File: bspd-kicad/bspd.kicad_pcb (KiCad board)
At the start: 2 copper layers, 6 parts

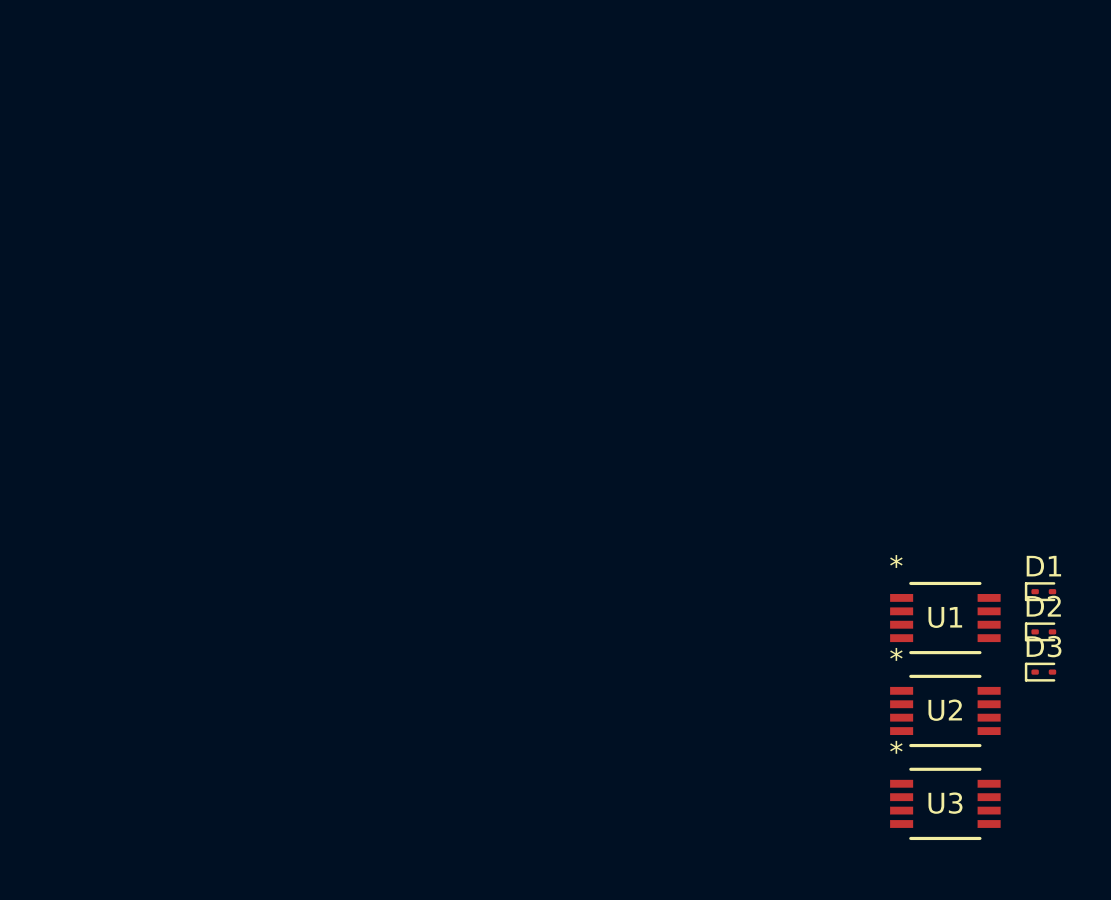
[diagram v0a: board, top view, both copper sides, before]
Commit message: fixed foot print, added power and connector
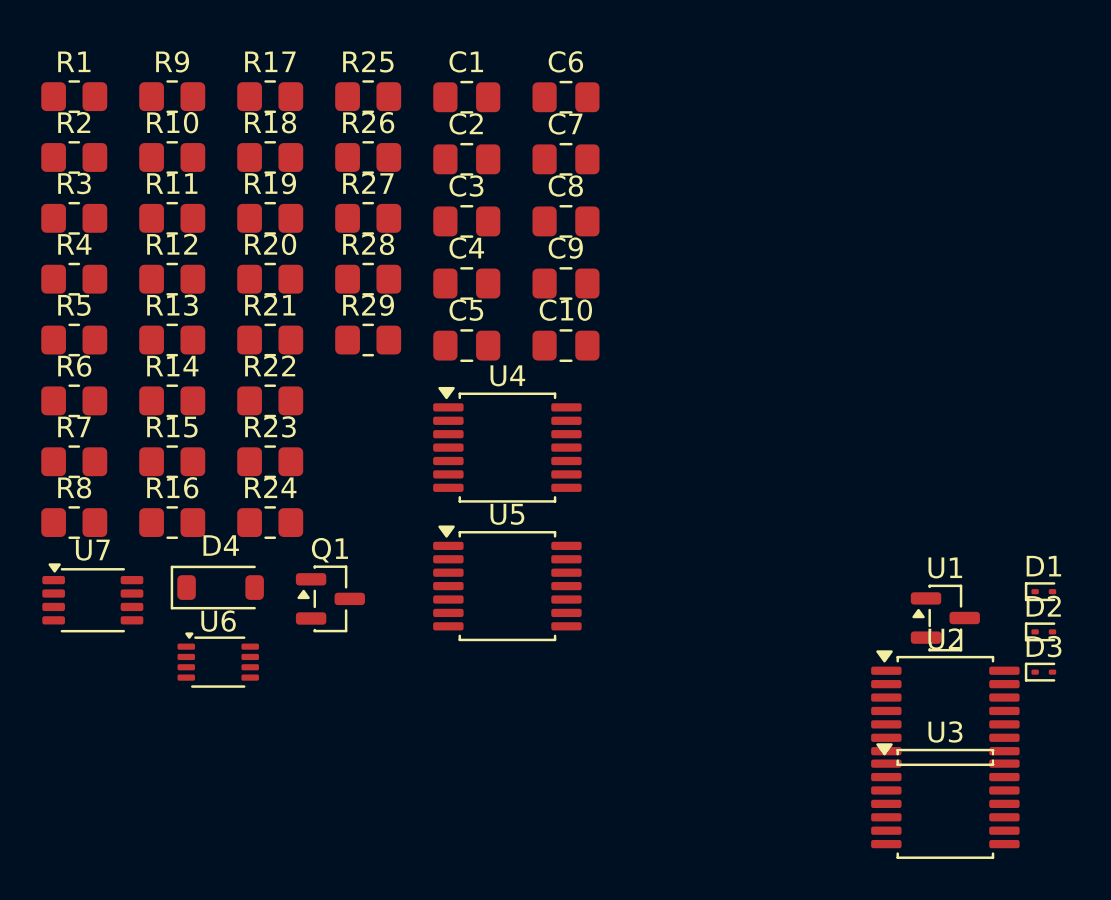
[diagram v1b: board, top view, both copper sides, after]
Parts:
- added C1: 1uF, Capacitor_SMD:C_0805_2012Metric_Pad1.18x1.45mm_HandSolder, F.Cu at (47.2, 34.5)
- added C10: xuF, Capacitor_SMD:C_0805_2012Metric_Pad1.18x1.45mm_HandSolder, F.Cu at (52.0, 46.5)
- added C2: 1uF, Capacitor_SMD:C_0805_2012Metric_Pad1.18x1.45mm_HandSolder, F.Cu at (47.2, 37.5)
- added C3: 5uF, Capacitor_SMD:C_0805_2012Metric_Pad1.18x1.45mm_HandSolder, F.Cu at (47.2, 40.5)
- added C4: 1uF, Capacitor_SMD:C_0805_2012Metric_Pad1.18x1.45mm_HandSolder, F.Cu at (47.2, 43.5)
- added C5: 1uF, Capacitor_SMD:C_0805_2012Metric_Pad1.18x1.45mm_HandSolder, F.Cu at (47.2, 46.5)
- added C6: 1uF, Capacitor_SMD:C_0805_2012Metric_Pad1.18x1.45mm_HandSolder, F.Cu at (52.0, 34.5)
- added C7: 1uF, Capacitor_SMD:C_0805_2012Metric_Pad1.18x1.45mm_HandSolder, F.Cu at (52.0, 37.5)
- added C8: 1uF, Capacitor_SMD:C_0805_2012Metric_Pad1.18x1.45mm_HandSolder, F.Cu at (52.0, 40.5)
- added C9: 1uF, Capacitor_SMD:C_0805_2012Metric_Pad1.18x1.45mm_HandSolder, F.Cu at (52.0, 43.5)
- added D4: 1N4148W, Diode_SMD:D_SOD-123, F.Cu at (35.2, 58.3)
- added Q1: AO3400A, Package_TO_SOT_SMD:SOT-23, F.Cu at (40.5, 58.8)
- added R1: 10k, Resistor_SMD:R_0805_2012Metric_Pad1.20x1.40mm_HandSolder, F.Cu at (28.1, 34.5)
- added R10: 10k, Resistor_SMD:R_0805_2012Metric_Pad1.20x1.40mm_HandSolder, F.Cu at (32.9, 37.4)
- added R11: 150k, Resistor_SMD:R_0805_2012Metric_Pad1.20x1.40mm_HandSolder, F.Cu at (32.9, 40.4)
- added R12: 150k, Resistor_SMD:R_0805_2012Metric_Pad1.20x1.40mm_HandSolder, F.Cu at (32.9, 43.3)
- added R13: 5.1k, Resistor_SMD:R_0805_2012Metric_Pad1.20x1.40mm_HandSolder, F.Cu at (32.9, 46.3)
- added R14: 150k, Resistor_SMD:R_0805_2012Metric_Pad1.20x1.40mm_HandSolder, F.Cu at (32.9, 49.2)
- added R15: 10k, Resistor_SMD:R_0805_2012Metric_Pad1.20x1.40mm_HandSolder, F.Cu at (32.9, 52.2)
- added R16: 150k, Resistor_SMD:R_0805_2012Metric_Pad1.20x1.40mm_HandSolder, F.Cu at (32.9, 55.1)
- added R17: 5.1k, Resistor_SMD:R_0805_2012Metric_Pad1.20x1.40mm_HandSolder, F.Cu at (37.6, 34.5)
- added R18: 150k, Resistor_SMD:R_0805_2012Metric_Pad1.20x1.40mm_HandSolder, F.Cu at (37.6, 37.4)
- added R19: 150k, Resistor_SMD:R_0805_2012Metric_Pad1.20x1.40mm_HandSolder, F.Cu at (37.6, 40.4)
- added R2: 5.1k, Resistor_SMD:R_0805_2012Metric_Pad1.20x1.40mm_HandSolder, F.Cu at (28.1, 37.4)
- added R20: 5.1k, Resistor_SMD:R_0805_2012Metric_Pad1.20x1.40mm_HandSolder, F.Cu at (37.6, 43.3)
- added R21: 54.9k, Resistor_SMD:R_0805_2012Metric_Pad1.20x1.40mm_HandSolder, F.Cu at (37.6, 46.3)
- added R22: 21.5k, Resistor_SMD:R_0805_2012Metric_Pad1.20x1.40mm_HandSolder, F.Cu at (37.6, 49.2)
- added R23: 100k, Resistor_SMD:R_0805_2012Metric_Pad1.20x1.40mm_HandSolder, F.Cu at (37.6, 52.2)
- added R24: 4.99k, Resistor_SMD:R_0805_2012Metric_Pad1.20x1.40mm_HandSolder, F.Cu at (37.6, 55.1)
- added R25: 5.49k, Resistor_SMD:R_0805_2012Metric_Pad1.20x1.40mm_HandSolder, F.Cu at (42.4, 34.5)
- added R26: 7.15k, Resistor_SMD:R_0805_2012Metric_Pad1.20x1.40mm_HandSolder, F.Cu at (42.4, 37.4)
- added R27: 100k, Resistor_SMD:R_0805_2012Metric_Pad1.20x1.40mm_HandSolder, F.Cu at (42.4, 40.4)
- added R28: 45.3k, Resistor_SMD:R_0805_2012Metric_Pad1.20x1.40mm_HandSolder, F.Cu at (42.4, 43.3)
- added R29: x, Resistor_SMD:R_0805_2012Metric_Pad1.20x1.40mm_HandSolder, F.Cu at (42.4, 46.3)
- added R3: 5.1k, Resistor_SMD:R_0805_2012Metric_Pad1.20x1.40mm_HandSolder, F.Cu at (28.1, 40.4)
- added R4: 150k, Resistor_SMD:R_0805_2012Metric_Pad1.20x1.40mm_HandSolder, F.Cu at (28.1, 43.3)
- added R5: 5.1k, Resistor_SMD:R_0805_2012Metric_Pad1.20x1.40mm_HandSolder, F.Cu at (28.1, 46.3)
- added R6: 150k, Resistor_SMD:R_0805_2012Metric_Pad1.20x1.40mm_HandSolder, F.Cu at (28.1, 49.2)
- added R7: 150k, Resistor_SMD:R_0805_2012Metric_Pad1.20x1.40mm_HandSolder, F.Cu at (28.1, 52.2)
- added R8: 150k, Resistor_SMD:R_0805_2012Metric_Pad1.20x1.40mm_HandSolder, F.Cu at (28.1, 55.1)
- added R9: 5.1k, Resistor_SMD:R_0805_2012Metric_Pad1.20x1.40mm_HandSolder, F.Cu at (32.9, 34.5)
- added U4: ~, bspd:TLV1704, F.Cu at (49.1, 51.5)
- added U5: ~, bspd:TLV1704, F.Cu at (49.1, 58.2)
- added U6: SN74LVC3G14DCUR, bspd:SN74LVC3G14DCUR, F.Cu at (35.1, 61.9)
- added U7: SN74LVC2G00DCTR, bspd:SN74LVC2G00DCTR, F.Cu at (29.0, 58.9)
- U1: value ~ -> MCP1703T-5002E/CB; footprint bspd:TLV3202AQDGKRQ1 -> bspd:MCP1703T-5002E-CB
- U2, U3: footprint bspd:TLV3202AQDGKRQ1 -> bspd:TLV1704
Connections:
- U1 pad 1: Net-(D4-A) -> Earth
- U1 pad 2: TPS1 -> +5V
- U1 pad 3: +4.5V -> +12V
- U2 pad 1: Net-(D6-A) -> TPS1_FAULT
- U2 pad 2: TPS2 -> TPS1_FAULT
- U2 pad 3: +4.5V -> +5V
- U2 pad 4: Earth -> TPS1
- U2 pad 5: TPS2 -> +4V5
- U2 pad 6: +0.5V -> +0V45
- U2 pad 7: Net-(D7-A) -> TPS1
- U2 pad 8: +5V -> TPS2
- U3 pad 1: Net-(D8-A) -> BPS_FAULT
- U3 pad 2: BPS -> BPS_FAULT
- U3 pad 3: +4.5V -> +5V
- U3 pad 4: Earth -> BPS
- U3 pad 5: BPS -> +4V5
- U3 pad 6: +0.5V -> +0V45
- U3 pad 7: Net-(D9-A) -> BPS
- U3 pad 8: +5V -> BPS

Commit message: Begun layout
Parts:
- moved U1 66.5 mm to (19.7, 16.7)
- moved R9 65.5 mm to (63.2, 92.5), turned to -90 degrees
- moved R19 64.6 mm to (78.0, 90.8), turned to 90 degrees
- moved R5 64.2 mm to (81.5, 82.0), turned to 90 degrees
- moved R3 57.6 mm to (53.2, 92.2), turned to -90 degrees
- moved C6 57.1 mm to (73.2, 87.5)
- moved R14 57.0 mm to (72.2, 90.5), turned to 90 degrees
- moved C7 56.5 mm to (37.0, 92.0), turned to -90 degrees
- moved R11 55.9 mm to (56.5, 91.0), turned to 180 degrees
- moved R13 54.8 mm to (56.5, 95.8), turned to 180 degrees
- moved R18 54.6 mm to (78.0, 74.2), turned to -90 degrees
- moved D3 53.4 mm to (31.5, 93.2), turned to 90 degrees
- moved R6 52.4 mm to (56.5, 93.2), turned to 180 degrees
- moved C9 51.6 mm to (79.0, 87.5)
- moved D2 50.2 mm to (31.5, 85.2), turned to 90 degrees
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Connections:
- C3 pad 1: Net-(U4C-+) -> Net-(U5A-+)
- C6 pad 1: Net-(U4D-+) -> Net-(U5B-+)
- C8 pad 1: Net-(U5A-+) -> Net-(U5C-+)
- C9 pad 1: Net-(U5B-+) -> Net-(U5D-+)
- R14 pad 2: Net-(U4D-+) -> Net-(U5B-+)
- R18 pad 2: Net-(U5A-+) -> Net-(U5C-+)
- R19 pad 2: Net-(U5B-+) -> Net-(U5D-+)
- R8 pad 2: Net-(U4C-+) -> Net-(U5A-+)
- U4 pad 10: +2V5 -> Earth
- U4 pad 11: Net-(U4D-+) -> +5V
- U4 pad 13: FAULT -> unconnected-(U4-Pad13)
- U4 pad 14: FAULT -> unconnected-(U4-Pad14)
- U4 pad 8: +2V5 -> Earth
- U4 pad 9: Net-(U4C-+) -> +5V
- U5 pad 10: Earth -> +2V5
- U5 pad 11: +5V -> Net-(U5D-+)
- U5 pad 13: unconnected-(U5-Pad13) -> FAULT
- U5 pad 14: unconnected-(U5-Pad14) -> FAULT
- U5 pad 8: Earth -> +2V5
- U5 pad 9: +5V -> Net-(U5C-+)

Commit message: Switched to D latch chip
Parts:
- removed U6: SN74LVC3G14DCUR, bspd:SN74LVC3G14DCUR
- C10: value xuF -> 2.2uF
- R29: value x -> 330k
- U7: value SN74LVC2G00DCTR -> SN74LVC2G14DBVR; footprint bspd:SN74LVC2G00DCTR -> bspd:SN74LVC2G14DBVR
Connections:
- U7 pad 1: Net-(U7A-A) -> Net-(D4-A)
- U7 pad 2: Net-(U7A-B) -> Earth
- U7 pad 3: Net-(U7A-B) -> Net-(U7-Pad3)
- U7 pad 4: Earth -> Net-(U8A-~{R})
- U7 pad 5: Net-(Q1-G) -> +5V
- U7 pad 6: Net-(U7B-B) -> Net-(U7-Pad3)

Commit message: Fixed latch and added indicator LEDs
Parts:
- removed C10: 2.2uF, Capacitor_SMD:C_0805_2012Metric_Pad1.18x1.45mm_HandSolder
- removed Q1: AO3400A, Package_TO_SOT_SMD:SOT-23
- added C11: 5uF, Capacitor_SMD:C_0805_2012Metric_Pad1.18x1.45mm_HandSolder, F.Cu at (24.9, 54.5)
- added D10: AP2012EC, bspd:AP2012EC, F.Cu at (76.4, 48.2)
- added D11: AP2012EC, bspd:AP2012EC, F.Cu at (76.4, 51.8)
- added D5: AP2012EC, bspd:AP2012EC, F.Cu at (76.4, 30.8)
- added D6: AP2012EC, bspd:AP2012EC, F.Cu at (76.4, 34.2)
- added D7: AP2012EC, bspd:AP2012EC, F.Cu at (76.4, 37.8)
- added D8: AP2012EC, bspd:AP2012EC, F.Cu at (76.4, 41.2)
- added D9: AP2012EC, bspd:AP2012EC, F.Cu at (76.4, 44.8)
- added Q2: AO3401A, Package_TO_SOT_SMD:SOT-23, F.Cu at (5.31, 59.2)
- added R30: 150k, Resistor_SMD:R_0805_2012Metric_Pad1.20x1.40mm_HandSolder, F.Cu at (24.9, 57.5)
- added R31: 300, Resistor_SMD:R_0805_2012Metric_Pad1.20x1.40mm_HandSolder, F.Cu at (71.8, 30.8)
- added R32: 300, Resistor_SMD:R_0805_2012Metric_Pad1.20x1.40mm_HandSolder, F.Cu at (71.8, 34.2)
- added R33: 300, Resistor_SMD:R_0805_2012Metric_Pad1.20x1.40mm_HandSolder, F.Cu at (71.8, 37.8)
- added R34: 300, Resistor_SMD:R_0805_2012Metric_Pad1.20x1.40mm_HandSolder, F.Cu at (71.8, 41.2)
- added R35: 300, Resistor_SMD:R_0805_2012Metric_Pad1.20x1.40mm_HandSolder, F.Cu at (71.8, 44.8)
- added R36: 300, Resistor_SMD:R_0805_2012Metric_Pad1.20x1.40mm_HandSolder, F.Cu at (71.8, 48.2)
- added R37: 300, Resistor_SMD:R_0805_2012Metric_Pad1.20x1.40mm_HandSolder, F.Cu at (71.8, 51.8)
- added R38: 300, Resistor_SMD:R_0805_2012Metric_Pad1.20x1.40mm_HandSolder, F.Cu at (-0.25, 58.2)
- added RV4: 3313J-1-103E, bspd:3313J-1-103E, F.Cu at (16.5, 49.6)
- added RV5: 3313J-1-103E, bspd:3313J-1-103E, F.Cu at (21.4, 49.6)
- added RV6: 3313J-1-103E, bspd:3313J-1-103E, F.Cu at (26.4, 49.6)
- added U6: SN74HC74DR, bspd:SN74HC74DR, F.Cu at (18.2, 58.3)
- added U8: SN74LVC3G14DCUR, bspd:SN74LVC3G14DCUR, F.Cu at (84.5, 33.5)
- added U9: SN74LVC3G14DCUR, bspd:SN74LVC3G14DCUR, F.Cu at (84.5, 44.0)
- R29: value 330k -> 150k
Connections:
- net Net-(R11-Pad2) renamed TPSx10%
- net Net-(U4B-+) renamed HB
- R29 pad 1: Net-(D4-A) -> Net-(R29-Pad1)
- R29 pad 2: +5V -> Net-(D4-A)

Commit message: Started layout, emphasis on looking good
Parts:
- removed RV6: 3313J-1-103E, bspd:3313J-1-103E
- removed U6: SN74HC74DR, bspd:SN74HC74DR
- added C10: 4.7uF, Capacitor_SMD:C_0805_2012Metric_Pad1.18x1.45mm_HandSolder, F.Cu at (102.9, 49.7)
- added C12: 100nF, Capacitor_SMD:C_0805_2012Metric_Pad1.18x1.45mm_HandSolder, F.Cu at (13.5, 16.0)
- added C13: 100nF, Capacitor_SMD:C_0805_2012Metric_Pad1.18x1.45mm_HandSolder, F.Cu at (101.2, 60.5)
- added C14: 100nF, Capacitor_SMD:C_0805_2012Metric_Pad1.18x1.45mm_HandSolder, F.Cu at (101.2, 63.5)
- added C15: 100nF, Capacitor_SMD:C_0805_2012Metric_Pad1.18x1.45mm_HandSolder, F.Cu at (101.2, 66.5)
- added C16: 100nF, Capacitor_SMD:C_0805_2012Metric_Pad1.18x1.45mm_HandSolder, F.Cu at (101.2, 69.5)
- added C17: 100nF, Capacitor_SMD:C_0805_2012Metric_Pad1.18x1.45mm_HandSolder, F.Cu at (101.2, 72.6)
- added C18: 100nF, Capacitor_SMD:C_0805_2012Metric_Pad1.18x1.45mm_HandSolder, F.Cu at (101.2, 75.6)
- added C19: 4.7uF, Capacitor_SMD:C_0805_2012Metric_Pad1.18x1.45mm_HandSolder, F.Cu at (98.9, 91.0)
- added C20: 100nF, Capacitor_SMD:C_0805_2012Metric_Pad1.18x1.45mm_HandSolder, F.Cu at (98.9, 94.0)
- added C21: 100nF, Capacitor_SMD:C_0805_2012Metric_Pad1.18x1.45mm_HandSolder, F.Cu at (98.9, 97.0)
- added C22: 100nF, Capacitor_SMD:C_0805_2012Metric_Pad1.18x1.45mm_HandSolder, F.Cu at (98.9, 100.0)
- added C23: 100nF, Capacitor_SMD:C_0805_2012Metric_Pad1.18x1.45mm_HandSolder, F.Cu at (98.9, 103.0)
- added C24: 100nF, Capacitor_SMD:C_0805_2012Metric_Pad1.18x1.45mm_HandSolder, F.Cu at (103.7, 91.0)
- added C25: 100nF, Capacitor_SMD:C_0805_2012Metric_Pad1.18x1.45mm_HandSolder, F.Cu at (103.7, 94.0)
- added C26: 100nF, Capacitor_SMD:C_0805_2012Metric_Pad1.18x1.45mm_HandSolder, F.Cu at (103.7, 97.0)
- added C27: 100nF, Capacitor_SMD:C_0805_2012Metric_Pad1.18x1.45mm_HandSolder, F.Cu at (103.7, 100.0)
- added C28: 100nF, Capacitor_SMD:C_0805_2012Metric_Pad1.18x1.45mm_HandSolder, F.Cu at (103.7, 103.0)
- added D12: AP2012EC, bspd:AP2012EC, F.Cu at (103.0, 39.4)
- added D13: AP2012EC, bspd:AP2012EC, F.Cu at (103.0, 42.3)
- added D14: 1N4148W, Diode_SMD:D_SOD-123, F.Cu at (109.0, 99.5)
- added Q1: AO3401A, Package_TO_SOT_SMD:SOT-23, F.Cu at (102.9, 45.9)
- added R39: 47k, Resistor_SMD:R_0805_2012Metric_Pad1.20x1.40mm_HandSolder, F.Cu at (107.7, 45.2)
- added R40: 56k, Resistor_SMD:R_0805_2012Metric_Pad1.20x1.40mm_HandSolder, F.Cu at (107.7, 48.1)
- added RV1: 3313J-1-203E, bspd:3313J-1-103E, F.Cu at (96.0, 34.6)
- added RV2: 3313J-1-203E, bspd:3313J-1-103E, F.Cu at (100.9, 34.6)
- added RV3: 3313J-1-203E, bspd:3313J-1-103E, F.Cu at (105.9, 34.6)
- added SW1: CJS-1200TB1, bspd:CJS-1200TB1, F.Cu at (97.0, 41.4)
- added SW2: CJS-1200TB1, bspd:CJS-1200TB1, F.Cu at (97.0, 48.1)
- added U10: LM1117MP-5.0, Package_TO_SOT_SMD:SOT-223-3_TabPin2, F.Cu at (132.2, 71.8)
- C1: value 1uF -> 4.7uF
- C11: value 5uF -> 100nF
- C3: value 5uF -> 1uF
- C8, C9: value 1uF -> 10uF
- D1: value SZESD9B5.0ST5G -> 1N4148W; footprint Diode_SMD:D_SOD-923 -> Diode_SMD:D_SOD-123
- D4: value 1N4148W -> SZESD9B5.0ST5G; footprint Diode_SMD:D_SOD-123 -> Diode_SMD:D_SOD-923
- D5: value AP2012EC -> 1N4148W; footprint bspd:AP2012EC -> Diode_SMD:D_SOD-123
- D6: value AP2012EC -> SMBJ16A; footprint bspd:AP2012EC -> bspd:SMBJ16A
- Q2: value AO3401A -> AO3400A
- R23, R27: value 100k -> 150k
- R29: value 150k -> 500
- R31: value 300 -> 150k
- R32, R33, R34, R35, R36, R37, R38: value 300 -> 500
- RV4, RV5: value 3313J-1-103E -> 3313J-1-203E
- U1: value MCP1703T-5002E/CB -> ~; footprint bspd:MCP1703T-5002E-CB -> bspd:TLV1704
- U5: value ~ -> SN74HC74DR; footprint bspd:TLV1704 -> bspd:SN74HC74DR
- moved C1 101.0 mm to (29.2, 115.8), turned to -90 degrees
- moved R16 80.9 mm to (60.5, 16.3), turned to 90 degrees
- moved D3 78.4 mm to (43.5, 15.8)
- moved R15 78.4 mm to (57.5, 16.3), turned to -90 degrees
- moved C5 72.8 mm to (63.5, 16.2), turned to 90 degrees
- moved R12 69.4 mm to (48.5, 16.2), turned to 90 degrees
- moved D2 69.2 mm to (31.5, 16.0)
- moved R10 67.8 mm to (45.5, 16.2), turned to -90 degrees
- moved C3 61.4 mm to (51.5, 16.2)
- moved D6 60.4 mm to (124.0, 71.5), turned to 90 degrees
- moved R4 59.4 mm to (36.5, 16.2), turned to 90 degrees
- moved R1 59.0 mm to (33.5, 16.2), turned to -90 degrees
- moved R8 58.6 mm to (26.2, 114.8)
- moved R7 57.1 mm to (26.2, 117.0), turned to 180 degrees
- moved C11 56.8 mm to (30.5, 111.0), turned to 90 degrees
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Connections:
- C1 pad 1: Earth -> Net-(D1-K)
- C1 pad 2: +12V -> Earth
- C11 pad 1: Earth -> +5V
- C11 pad 2: Net-(D4-A) -> Earth
- C2 pad 1: Earth -> TPS1
- C2 pad 2: +5V -> Earth
- C3 pad 1: Net-(U5A-+) -> TPS2
- C4 pad 1: TPS1 -> Net-(U3B-+)
- C5 pad 1: TPS2 -> BPS
- C6 pad 1: Net-(U5B-+) -> Net-(U3C-+)
- C7 pad 1: BPS -> Net-(U3D-+)
- C8 pad 1: Net-(U5C-+) -> Earth
- C8 pad 2: Earth -> +12V
- C9 pad 1: Net-(U5D-+) -> Earth
- C9 pad 2: Earth -> +5V
- D1 pad 1: Earth -> Net-(D1-K)
- D1 pad 2: TPS1_RAW -> HB&10%
- D2 pad 2: TPS2_RAW -> TPS1_RAW
- D3 pad 2: BPS_RAW -> TPS2_RAW
- D4 pad 1: +5V -> Earth
- D4 pad 2: Net-(D4-A) -> BPS_RAW
- D5 pad 1: Net-(D5-K) -> +5V
- D5 pad 2: LATCH_LED -> Net-(D5-A)
- D6 pad 1: Net-(D6-K) -> +12V
- D6 pad 2: Net-(D6-A) -> Earth
- D7 pad 2: Net-(D7-A) -> LATCH_LED
- Q2 pad 2: +12V -> Earth
- Q2 pad 3: SC_OUT -> Net-(Q2-D)
- R11 pad 1: HB -> Net-(U4B-+)
- R14 pad 2: Net-(U5B-+) -> Net-(U3B-+)
- R18 pad 2: Net-(U5C-+) -> Net-(U3C-+)
- R19 pad 2: Net-(U5D-+) -> Net-(U3D-+)
- R23 pad 1: +5V -> +2V5
- R23 pad 2: +2V5 -> +5V
- R27 pad 1: +2V5 -> Earth
- R27 pad 2: Earth -> +2V5
- R29 pad 1: Net-(R29-Pad1) -> Net-(U5A-Q)
- R29 pad 2: Net-(D4-A) -> Net-(Q2-G)
- R3 pad 2: Net-(R3-Pad2) -> HB
- R30 pad 2: Net-(R29-Pad1) -> Net-(D5-A)
- R31 pad 1: Net-(D5-K) -> Earth
- R31 pad 2: Earth -> Net-(Q2-G)
- R32 pad 1: Net-(D6-K) -> Net-(D7-K)
- R33 pad 1: Net-(D7-K) -> Net-(D8-K)
- R34 pad 1: Net-(D8-K) -> Net-(D9-K)
- R35 pad 1: Net-(D9-K) -> Net-(D10-K)
- R36 pad 1: Net-(D10-K) -> Net-(D11-K)
- R37 pad 1: Net-(D11-K) -> Net-(D12-K)
- R38 pad 2: Net-(Q2-G) -> Earth
- R6 pad 1: HB -> Net-(U4B-+)
- R6 pad 2: Net-(R3-Pad2) -> HB
- R8 pad 2: Net-(U5A-+) -> Net-(D1-K)
- RV4 pad 2: HB_THRESH -> V_THL_VAR
- RV5 pad 2: TPS1_THRESH -> V_THH_VAR
- U1 pad 1: Earth -> TPS1_FAULT
- U1 pad 2: +5V -> TPS1_FAULT
- U1 pad 3: +12V -> +5V
- U2 pad 1: TPS1_FAULT -> BPS_FAULT
- U2 pad 10: +0V45 -> TPS1
- U2 pad 11: TPS2 -> TPS1_THRESH
- U2 pad 13: TPS2_FAULT -> TPSx10%
- U2 pad 14: TPS2_FAULT -> HB
- U2 pad 2: TPS1_FAULT -> BPS_FAULT
- U2 pad 4: TPS1 -> BPS
- U2 pad 5: +4V5 -> V_THH
- U2 pad 6: +0V45 -> V_THL
- U2 pad 7: TPS1 -> BPS
- U2 pad 8: TPS2 -> BPS
- U2 pad 9: +4V5 -> HB_THRESH
- U3 pad 1: BPS_FAULT -> FAULT
- U3 pad 10: TPS1 -> +2V5
- U3 pad 11: TPS1_THRESH -> Net-(U3D-+)
- U3 pad 13: TPSx10% -> FAULT
- U3 pad 14: Net-(R3-Pad2) -> FAULT
- U3 pad 2: BPS_FAULT -> FAULT
- U3 pad 4: BPS -> +2V5
- U3 pad 5: +4V5 -> Net-(D1-K)
- U3 pad 6: +0V45 -> +2V5
- U3 pad 7: BPS -> Net-(U3B-+)
- U3 pad 8: BPS -> +2V5
- U3 pad 9: HB_THRESH -> Net-(U3C-+)
- U4 pad 7: HB -> Net-(U4B-+)
- U5 pad 10: +2V5 -> +5V
- U5 pad 11: Net-(U5D-+) -> Earth
- U5 pad 13: FAULT -> +5V
- U5 pad 14: FAULT -> +5V
- U5 pad 2: FAULT -> Earth
- U5 pad 3: +5V -> Earth
- U5 pad 4: +2V5 -> Net-(U5A-~{PRE})
- U5 pad 5: Net-(U5A-+) -> Net-(U5A-Q)
- U5 pad 6: +2V5 -> LATCH_LED
- U5 pad 7: Net-(U5B-+) -> Earth
- U5 pad 8: +2V5 -> unconnected-(U5B-~{Q}-Pad8)
- U5 pad 9: Net-(U5C-+) -> unconnected-(U5B-Q-Pad9)
- U7 pad 1: Net-(D4-A) -> Net-(D5-A)
- U7 pad 4: Net-(U6A-~{PRE}) -> Net-(U5A-~{PRE})
- U8 pad 2: Net-(D8-A) -> Net-(D13-A)
- U8 pad 5: Net-(D7-A) -> Net-(D10-A)
- U8 pad 7: Net-(D6-A) -> Net-(D8-A)
- U9 pad 2: Net-(D11-A) -> Net-(D12-A)
- U9 pad 5: Net-(D10-A) -> Net-(D11-A)
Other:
- board text added: "BPS"
- board text added: "TPS1"
- board text added: "TPS2"

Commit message: Layout progress
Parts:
- added TP1: TPS1, TestPoint:TestPoint_Keystone_5000-5004_Miniature, F.Cu at (129.2, 48.8)
- added TP2: TPS2, TestPoint:TestPoint_Keystone_5000-5004_Miniature, F.Cu at (141.2, 48.5)
- added TP3: BPS, TestPoint:TestPoint_Keystone_5000-5004_Miniature, F.Cu at (153.0, 48.5)
- added TP4: +0V45, TestPoint:TestPoint_Keystone_5000-5004_Miniature, F.Cu at (125.5, 18.5)
- added TP5: +1V25, TestPoint:TestPoint_Keystone_5000-5004_Miniature, F.Cu at (134.0, 18.2)
- added TP6: +2V5, TestPoint:TestPoint_Keystone_5000-5004_Miniature, F.Cu at (141.0, 18.5)
- added TP7: +4V5, TestPoint:TestPoint_Keystone_5000-5004_Miniature, F.Cu at (148.2, 18.2)
- moved R38 210.8 mm to (208.8, 85.5)
- moved R30 176.8 mm to (201.2, 45.8)
- moved R29 169.5 mm to (217.5, 42.8)
- moved Q2 168.9 mm to (173.5, 44.2)
- moved U7 163.6 mm to (198.2, 49.8)
- moved R6 162.7 mm to (202.1, 20.6), turned to -90 degrees
- moved C1 162.6 mm to (165.0, 26.2)
- moved C11 162.6 mm to (166.2, 21.5)
- moved C4 162.6 mm to (168.8, 28.8)
- moved C6 162.6 mm to (178.5, 25.2)
- moved C7 162.6 mm to (178.5, 22.8)
- moved D1 162.6 mm to (162.5, 23.0)
- moved R14 162.6 mm to (171.8, 27.8)
- moved R18 162.6 mm to (177.6, 28.3)
- moved R19 162.6 mm to (177.5, 19.8)
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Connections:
- R11 pad 1: Net-(U4B-+) -> Net-(U4D-+)
- R6 pad 1: Net-(U4B-+) -> Net-(U4D-+)
- U2 pad 10: TPS1 -> Earth
- U2 pad 11: TPS1_THRESH -> +5V
- U2 pad 13: TPSx10% -> unconnected-(U2-Pad13)
- U2 pad 14: HB -> unconnected-(U2-Pad14)
- U2 pad 8: BPS -> Earth
- U2 pad 9: HB_THRESH -> +5V
- U4 pad 1: HB&10% -> TPSx10%
- U4 pad 10: Earth -> +1V25
- U4 pad 11: +5V -> Net-(U4D-+)
- U4 pad 13: unconnected-(U4-Pad13) -> HB&10%
- U4 pad 14: unconnected-(U4-Pad14) -> TPSx10%
- U4 pad 2: TPSx10% -> HB
- U4 pad 4: TPS2_THRESH -> BPS
- U4 pad 5: TPS2 -> HB_THRESH
- U4 pad 6: +1V25 -> TPS1
- U4 pad 7: Net-(U4B-+) -> TPS1_THRESH
- U4 pad 8: Earth -> TPS2_THRESH
- U4 pad 9: +5V -> TPS2
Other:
- board text added: "0.45V"
- board text added: "1.25V"
- board text added: "12V->5V LDO"
- board text added: "2.5V"
- board text added: "4.5V"
- board text added: "Fixed Voltage References"
- board text added: "HB & 10%"
- board text added: "Input Filteration"
- board text added: "LED Indicator"
- board text added: "Latching"
- board text added: "Output Logic"
- board text added: "Timing Comparators"
- board text added: "Variable Voltage References"

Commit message: Layout progress
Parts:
- moved C14 182.3 mm to (20.4, 79.5)
- moved R11 182.3 mm to (26.1, 75.0)
- moved R13 182.3 mm to (23.6, 75.0)
- moved R3 182.3 mm to (20.4, 77.2)
- moved R6 182.3 mm to (28.1, 75.0)
- moved R9 182.3 mm to (32.4, 77.2)
- moved U4 182.3 mm to (26.9, 80.2)
- moved D10 123.6 mm to (89.9, 69.9)
- moved D11 123.6 mm to (89.9, 73.4)
- moved D12 123.6 mm to (89.9, 76.9)
- moved D13 123.6 mm to (89.9, 80.6)
- moved D7 123.6 mm to (89.9, 59.4)
- moved D8 123.6 mm to (89.9, 62.9)
- moved D9 123.6 mm to (89.9, 66.4)
- moved R32 123.6 mm to (85.2, 59.4)
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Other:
- board outline added: 100 x 80 mm
- board text added: "Window Comparators"
